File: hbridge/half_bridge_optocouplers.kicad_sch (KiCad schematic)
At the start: 5 parts, among them J20 Conn_01x04, J22 Conn_01x04, J23 Conn_01x04, J24 Conn_01x04, U5 Optocoupler_4chan

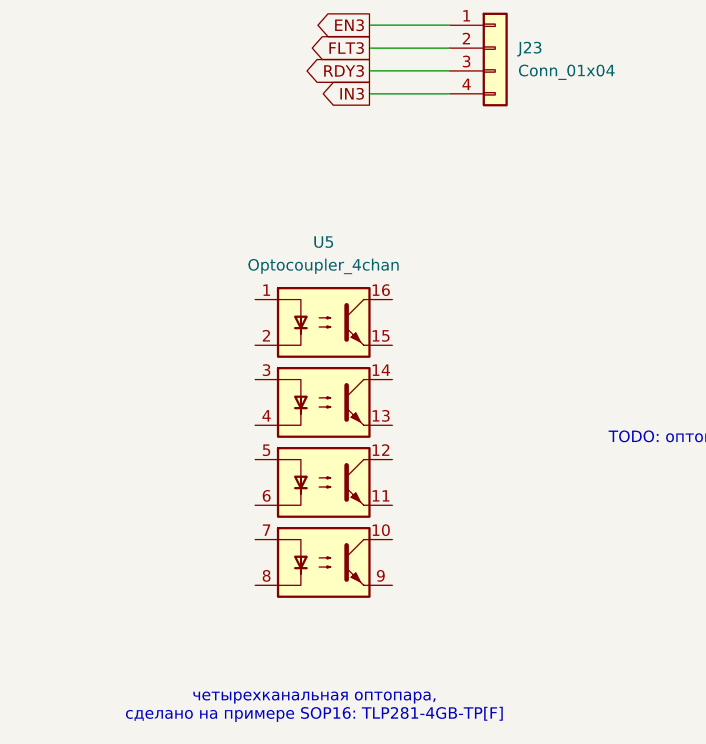
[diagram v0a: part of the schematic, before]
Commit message: Optocoupler schema changed.
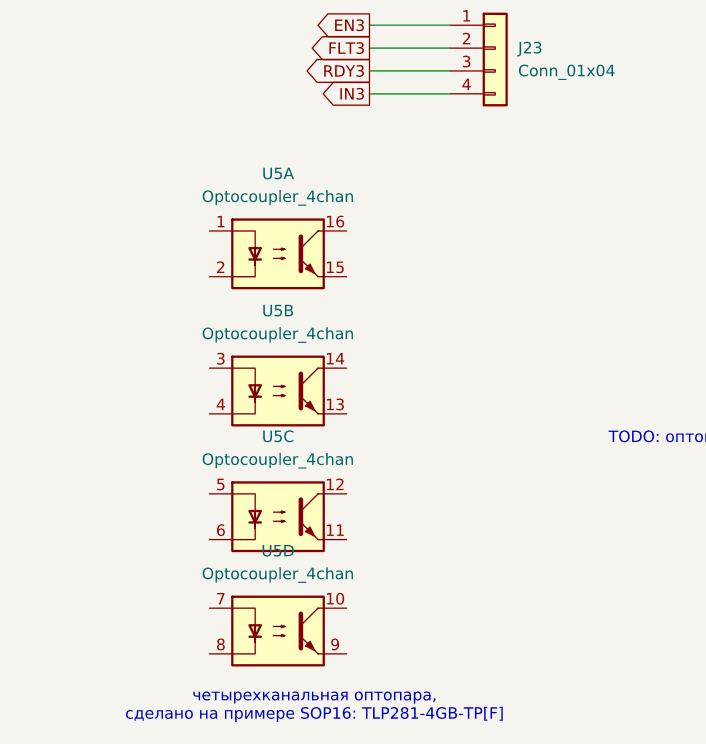
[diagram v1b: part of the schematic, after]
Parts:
- added unit 3 of U5
- added unit 2 of U5
- added unit 4 of U5

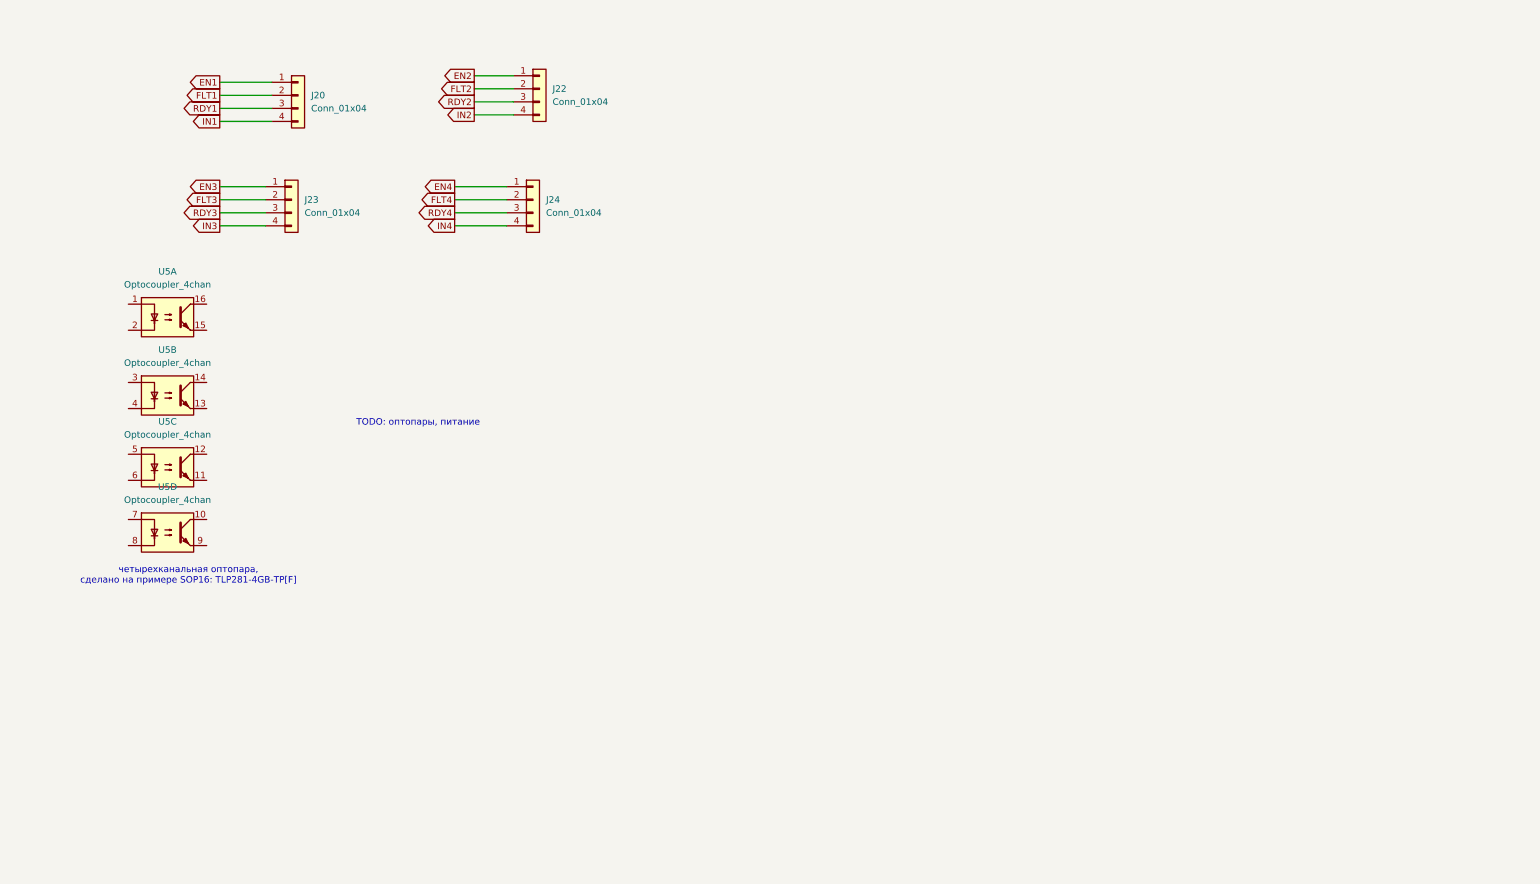
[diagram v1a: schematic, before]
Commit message: practice_pcb driver schematics changed (leds).
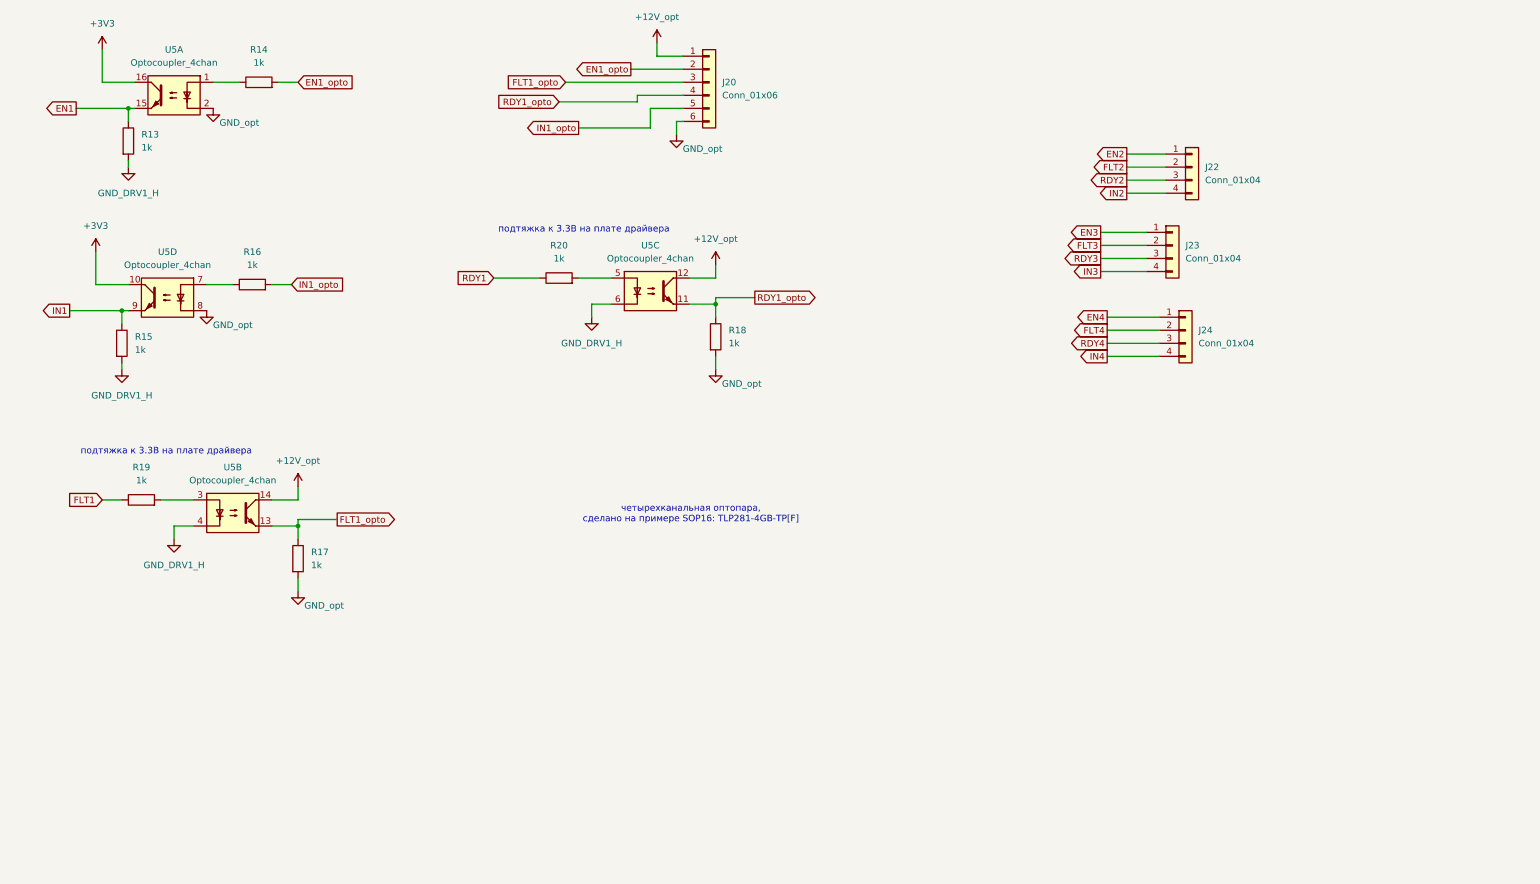
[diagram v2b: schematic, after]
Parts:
- removed J20: Conn_01x04, Connector_PinHeader_2.54mm:PinHeader_1x04_P2.54mm_Vertical, symbol Connector_Generic:Conn_01x04
- added J20: Conn_01x06, Connector_PinHeader_2.54mm:PinHeader_1x06_P2.54mm_Vertical, symbol Connector_Generic:Conn_01x06
- added R13, R15, R17, R18: 1k, Resistor_SMD:R_0402_1005Metric_Pad0.72x0.64mm_HandSolder, symbol Device:R
- added R14, R16, R19, R20: 1k, Resistor_SMD:R_0805_2012Metric_Pad1.20x1.40mm_HandSolder, symbol Device:R
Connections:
- net EN1: now also U5.15, R13.1
- net FLT1: now also R19.1
- net IN1: now also U5.9, R15.1
- net RDY1: now also R20.1
- net RDY1_opto: now reaches U5.11
- net RDY1_opto: now also J20.4 (Pin_4), R18.1
- net +12V_opt: now reaches U5.12
- net +12V_opt: now also U5.14, J20.1 (Pin_1)
- net at U5.5: now also R20.2
- net GND_DRV1_H: now reaches U5.6
- net GND_DRV1_H: now also U5.4, R13.2, R15.2
- net FLT1_opto: now reaches U5.13
- net FLT1_opto: now also J20.3 (Pin_3), R17.1
- net at U5.3: now also R19.2
- net +3V3: now reaches U5.10
- net +3V3: now also U5.16
- net at U5.7: now also R16.1
- net GND_opt: now reaches U5.8
- net GND_opt: now also U5.2, J20.6 (Pin_6), R17.2, R18.2
- net at U5.1: now also R14.1
- new net EN1_opto: J20.2 (Pin_2), R14.2
- new net IN1_opto: J20.5 (Pin_5), R16.2
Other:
- note added: "подтяжка к 3.3В на плате драйвера"
- note removed: "TODO: оптопары, питание"
- moved on the sheet: J22, J23, J24, U5A, U5B

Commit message: Driver board: castellated holes. SMD diode.
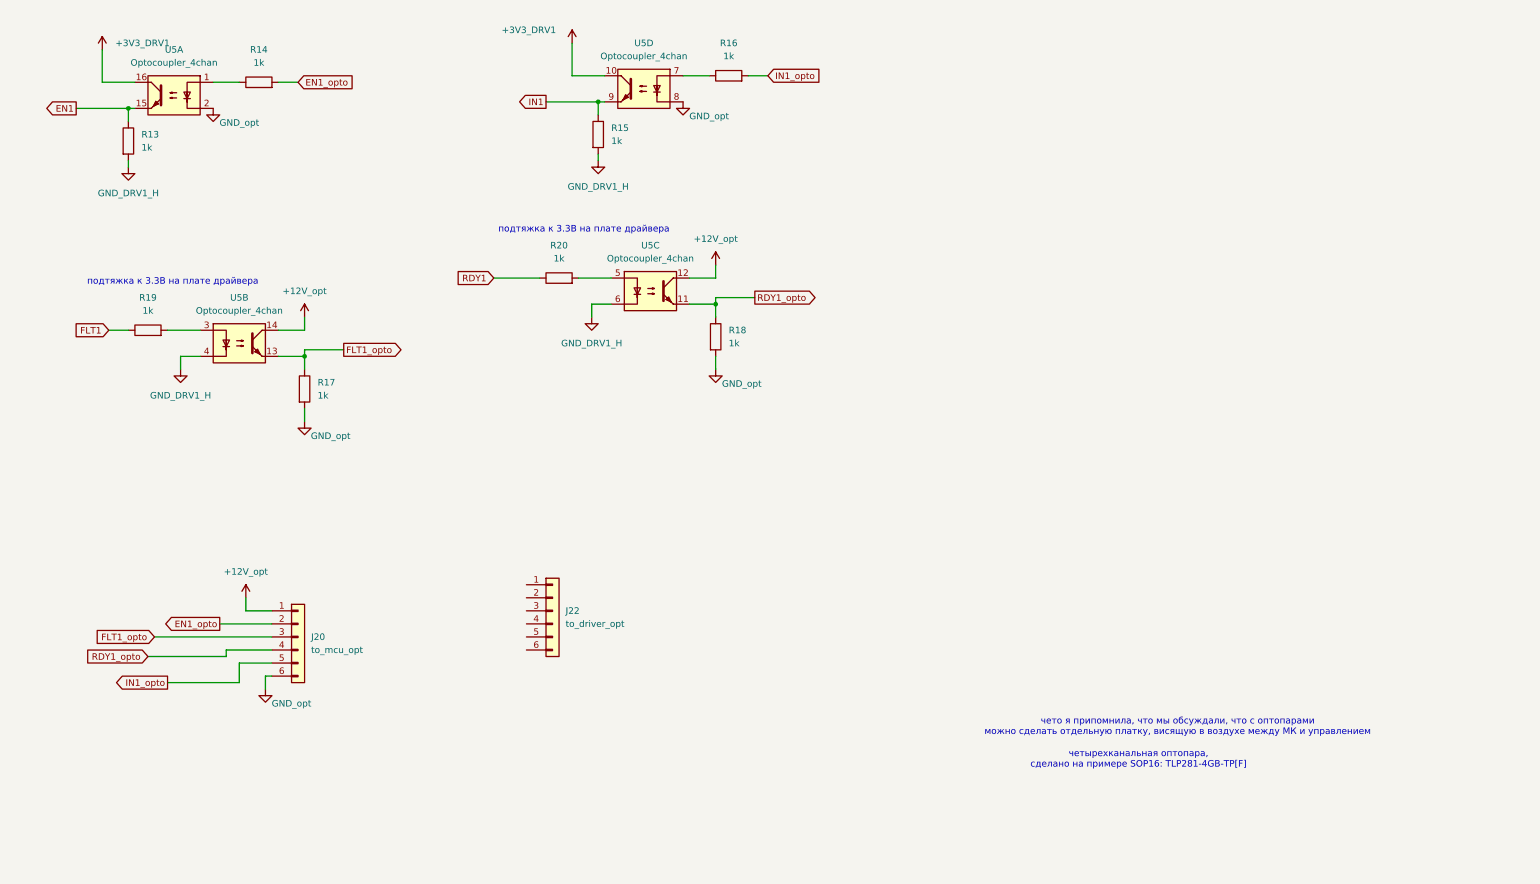
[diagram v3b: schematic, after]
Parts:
- removed J22, J23, J24: Conn_01x04, Connector_PinHeader_2.54mm:PinHeader_1x04_P2.54mm_Vertical, symbol Connector_Generic:Conn_01x04
- added J22: to_driver_opt, Connector_PinHeader_2.54mm:PinHeader_1x06_P2.54mm_Vertical, symbol Connector_Generic:Conn_01x06
- J20: value Conn_01x06 -> to_mcu_opt
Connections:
- net +3V3 renamed +3V3_DRV1
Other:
- note added: "чето я припомнила, что мы обсуждали, что с оптопарами можно сделать отдельную платку, висящую в воздухе между МК и управлением"
- moved on the sheet: J20, R15, R16, R17, R19, U5B, U5D

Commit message: Half-bridge board: driver defence circuit added.
Logical circuit on AND, NOT, RS-latch, Shift-register.
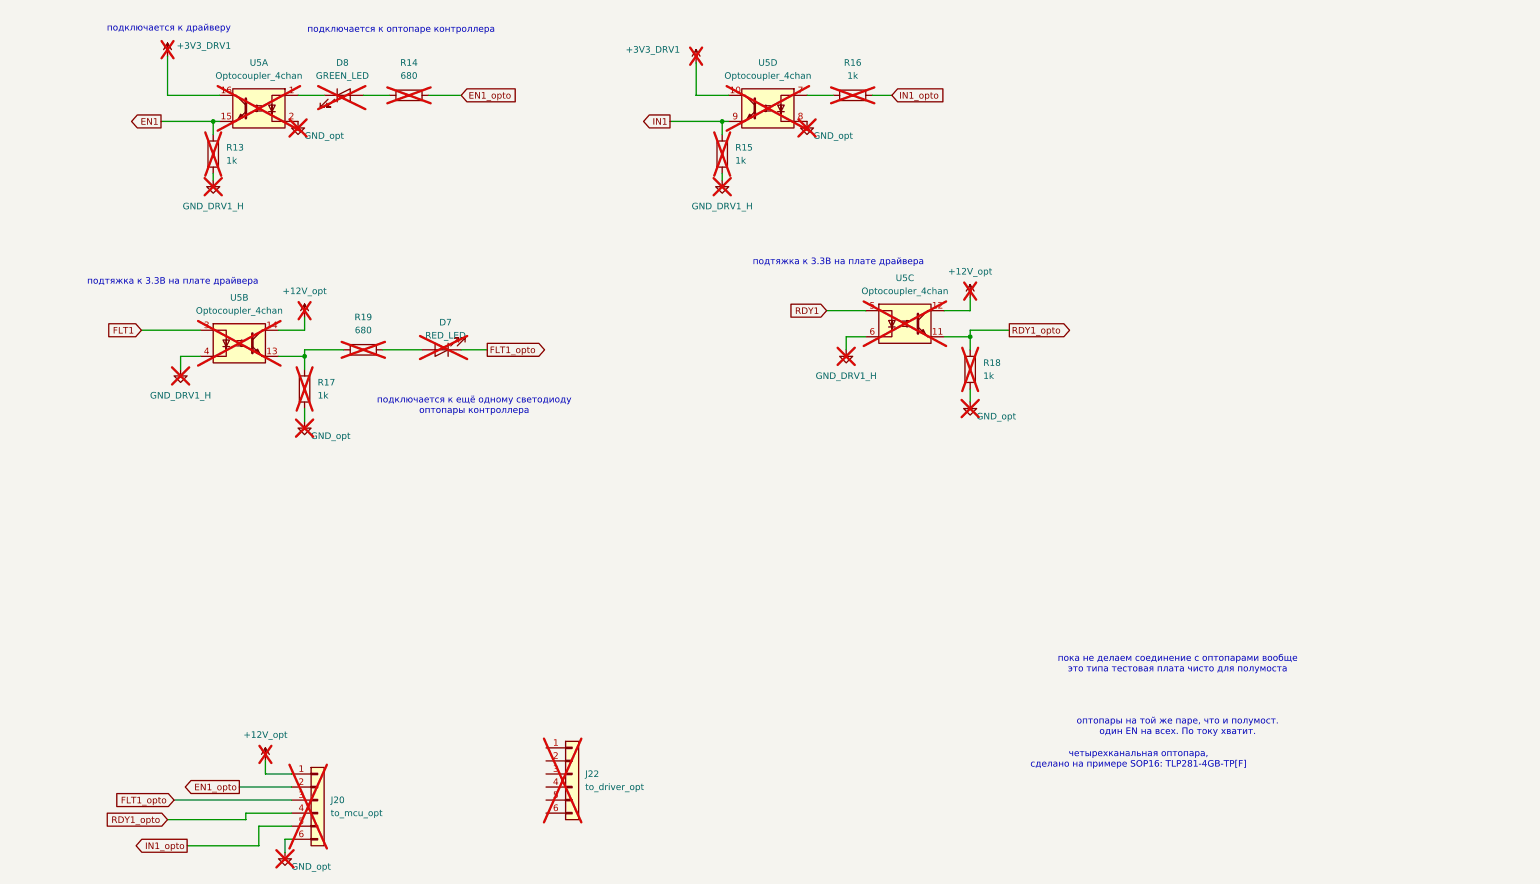
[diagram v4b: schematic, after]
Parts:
- removed R20: 1k, Resistor_SMD:R_0805_2012Metric_Pad1.20x1.40mm_HandSolder, symbol Device:R
- added D7: RED_LED, symbol Device:LED
- added D8: GREEN_LED, symbol Device:LED
- J20: footprint Connector_PinHeader_2.54mm:PinHeader_1x06_P2.54mm_Vertical -> Connector_PinHeader_2.54mm:PinHeader_1x06_P2.54mm_Horizontal; now not fitted; now left out of the parts list
- J22, R13, R15, R16, R17, R18, U5: now not fitted; now left out of the parts list
- R14: value 1k -> 680; now not fitted; now left out of the parts list
- R19: value 1k -> 680; footprint Resistor_SMD:R_0805_2012Metric_Pad1.20x1.40mm_HandSolder -> Resistor_SMD:R_0402_1005Metric_Pad0.72x0.64mm_HandSolder; now not fitted; now left out of the parts list
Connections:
- net FLT1: now also U5.3; no longer R19.1
- net FLT1_opto: now also D7.1 (K); no longer R17.1, U5.13
- net RDY1: now also U5.5
- net at R19.2: now also D7.2 (A); no longer U5.3
- net at U5.1: now also D8.1 (K); no longer R14.1
- new net: R17.1, R19.1, U5.13
- new net: D8.2 (A), R14.1
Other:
- note added: "оптопары на той же паре, что и полумост. один EN на всех. По току хватит."
- note added: "подключается к драйверу"
- note added: "подключается к ещё одному светодиоду оптопары контроллера"
- note added: "подключается к оптопаре контроллера"
- note added: "пока не делаем соединение с оптопарами вообще это типа тестовая плата чисто для полумоста"
- note removed: "чето я припомнила, что мы обсуждали, что с оптопарами можно сделать отдельную платку, висящую в воздухе между МК и управлением"
